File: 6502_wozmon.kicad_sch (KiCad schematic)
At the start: 37 parts, among them J1 Barrel_Jack_Switch_Pin3Ring, J2 DB9_Female, J3 "Switch", J4 Conn_01x08_Male, U1 7400, U2 W65C02, U3 28C256, U4 W65C51N, U5 62256, U6 MAX232, U7 65C22, U8 WC1602A, X1 GTXO-S14V, Y1 1.8432MHZ

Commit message: schematic updated to include debounced reset section; added barrel connector.
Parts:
- removed C1: 0.1u, Capacitor_THT:C_Disc_D5.0mm_W2.5mm_P5.00mm, symbol Device:C
- removed J3: "Switch", Connector_PinHeader_2.54mm:PinHeader_1x03_P2.54mm_Vertical, symbol Connector:Conn_01x03_Male
- removed R1: 1K, Resistor_THT:R_Axial_DIN0207_L6.3mm_D2.5mm_P10.16mm_Horizontal, symbol Device:R
- added C? (x2): C, symbol Device:C
- added C?: 10u, symbol Device:C
- added D?: LED, symbol Device:LED
- added J? (x2): Conn_01x03_Male, symbol Connector:Conn_01x03_Male
- added R?: 10K, symbol Device:R
- added R?: 330, symbol Device:R
- added R?: 1K, symbol Device:R
- added U? (x7): 74HC14, symbol 74xx:74HC14
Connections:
- net +5V: now also C?.1, C?.1, R?.2, U?.14 (VCC)
- net CLK: now also J4.1 (Pin_1); no longer J4.5 (Pin_5)
- net GND: now also J4.5 (Pin_5), J4.6 (Pin_6), J4.7 (Pin_7), J4.8 (Pin_8), C?.2, C?.2, C?.2, D?.1 (K), J?.3 (Pin_3), U?.11, U?.13, U?.5, U?.7 (GND), U?.9; no longer J4.1 (Pin_1), J4.2 (Pin_2), J4.3 (Pin_3), J4.4 (Pin_4)
- net RESET*: now also J4.2 (Pin_2), U?.4
- net TXD: now also J4.4 (Pin_4)
- net XTAL: no longer J4.6 (Pin_6)
- net MAX232_12: now reaches R7.1, U4.12 (RxD), U6.12 (R1OUT)
- net MAX232_12: now also J4.3 (Pin_3)
- new net: J?.1 (Pin_1), R?.1 (x2)
- new net: D?.2 (A), R?.2
- new net: R?.1, U?.2, U?.3
- new net: C?.1, R?.2, U?.1
- no-connect marks 48 -> 50
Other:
- note added: "DEBOUNCED RESET SECTION"
- note added: "Jx and Jy REPRESENT A FOUR-PIN BUTTON."
- moved on the sheet: J2, J4, U1D, U1E

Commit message: increment
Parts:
- removed LED_3, LED_4: LED, LED_THT:LED_D5.0mm, symbol Device:LED
- removed R7, R8: 220, Resistor_THT:R_Axial_DIN0207_L6.3mm_D2.5mm_P10.16mm_Horizontal, symbol Device:R
- C1, C10, C11: renamed from C?; footprint (none) -> Capacitor_THT:C_Disc_D5.0mm_W2.5mm_P5.00mm
- D3: renamed from D?; footprint (none) -> LED_THT:LED_D5.0mm
- J3, J5: renamed from J?; footprint (none) -> Connector_PinHeader_2.54mm:PinHeader_1x03_P2.54mm_Vertical
- R1, R6, R7: renamed from R?; footprint (none) -> Resistor_THT:R_Axial_DIN0207_L6.3mm_D2.5mm_P10.16mm_Horizontal
- U3: footprint Package_DIP:DIP-28_W15.24mm_Socket -> Socket:DIP_Socket-28_W11.9_W12.7_W15.24_W17.78_W18.5_3M_228-1277-00-0602J
- U5: footprint Socket:DIP_Socket-28_W11.9_W12.7_W15.24_W17.78_W18.5_3M_228-1277-00-0602J -> Package_DIP:DIP-28_W15.24mm_Socket
- U9: renamed from U?; footprint (none) -> Package_DIP:DIP-14_W7.62mm_Socket

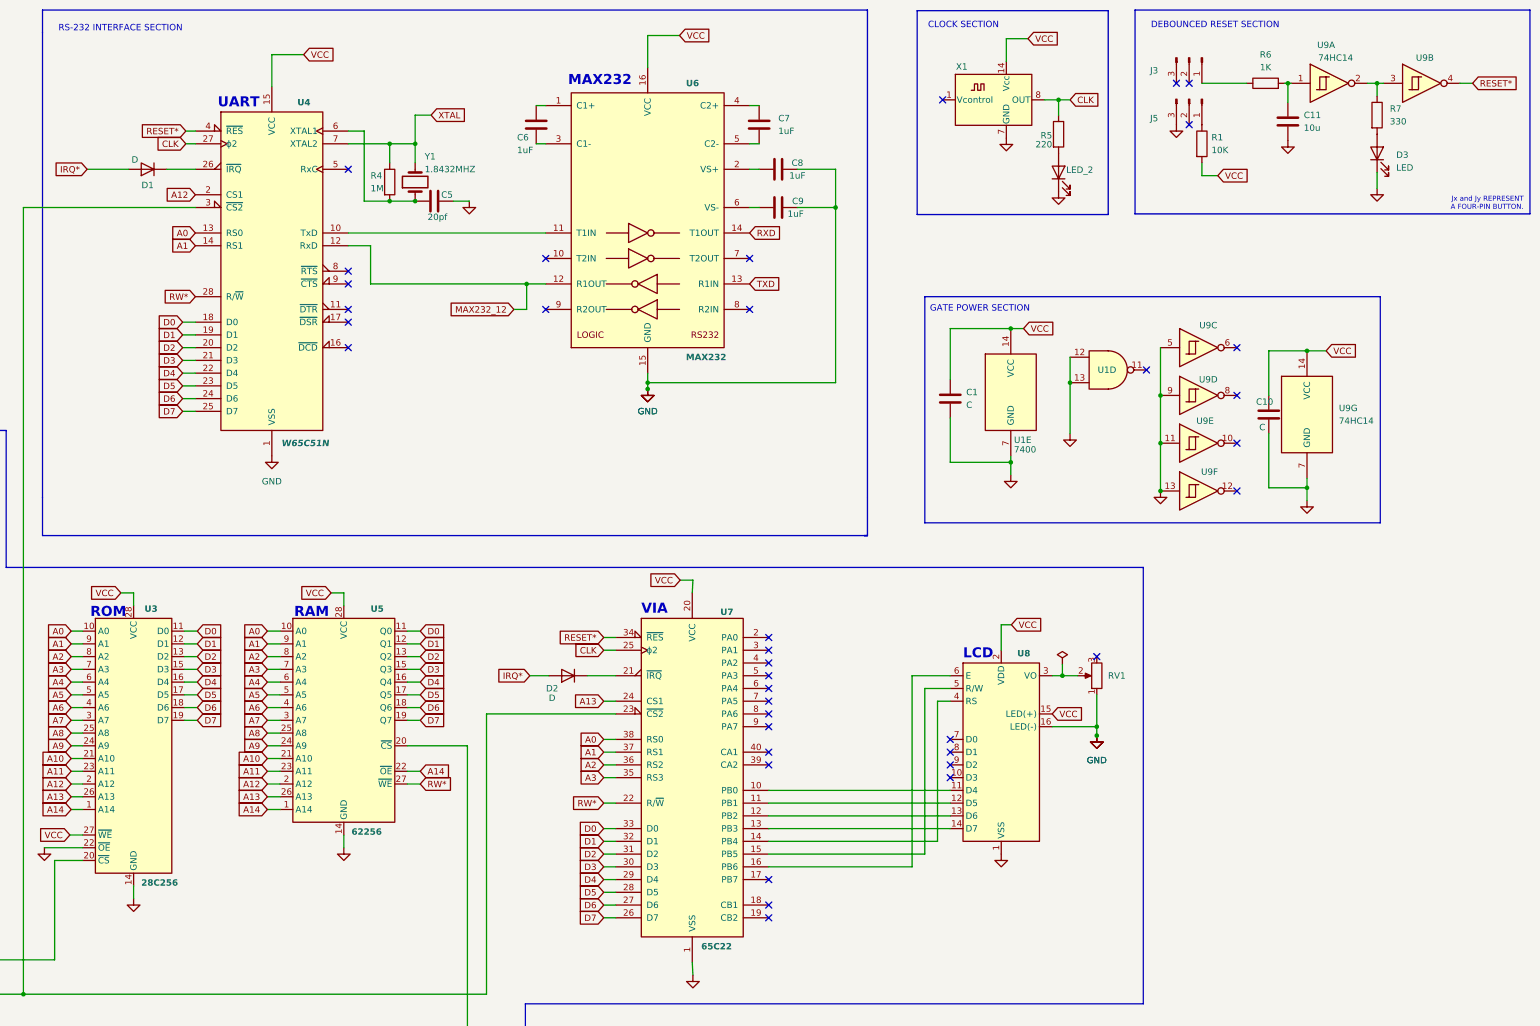
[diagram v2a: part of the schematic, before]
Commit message: 1.  Updated Files     A.  The pin headers being used as a switch were replaced with a proper button switch and footprint.         a.  The following were updated:             1.  6502_wozmon.kicad_pcb 	        2.  6502_wozmon.kicad_prl 2.  Notes     A.  The silkscreen for the RAM and ROM chips is reversed.         a.  This is becuase the footprints are reversed in the schematic editor.             1.  I switched the footprints, but this caused *37& clearance violations in the PCB editor.             2.  Fixing this would have required *substantial* re-routing.             3.  I decided for forego fixing this; I will accept this minor issue on the silkscreen.
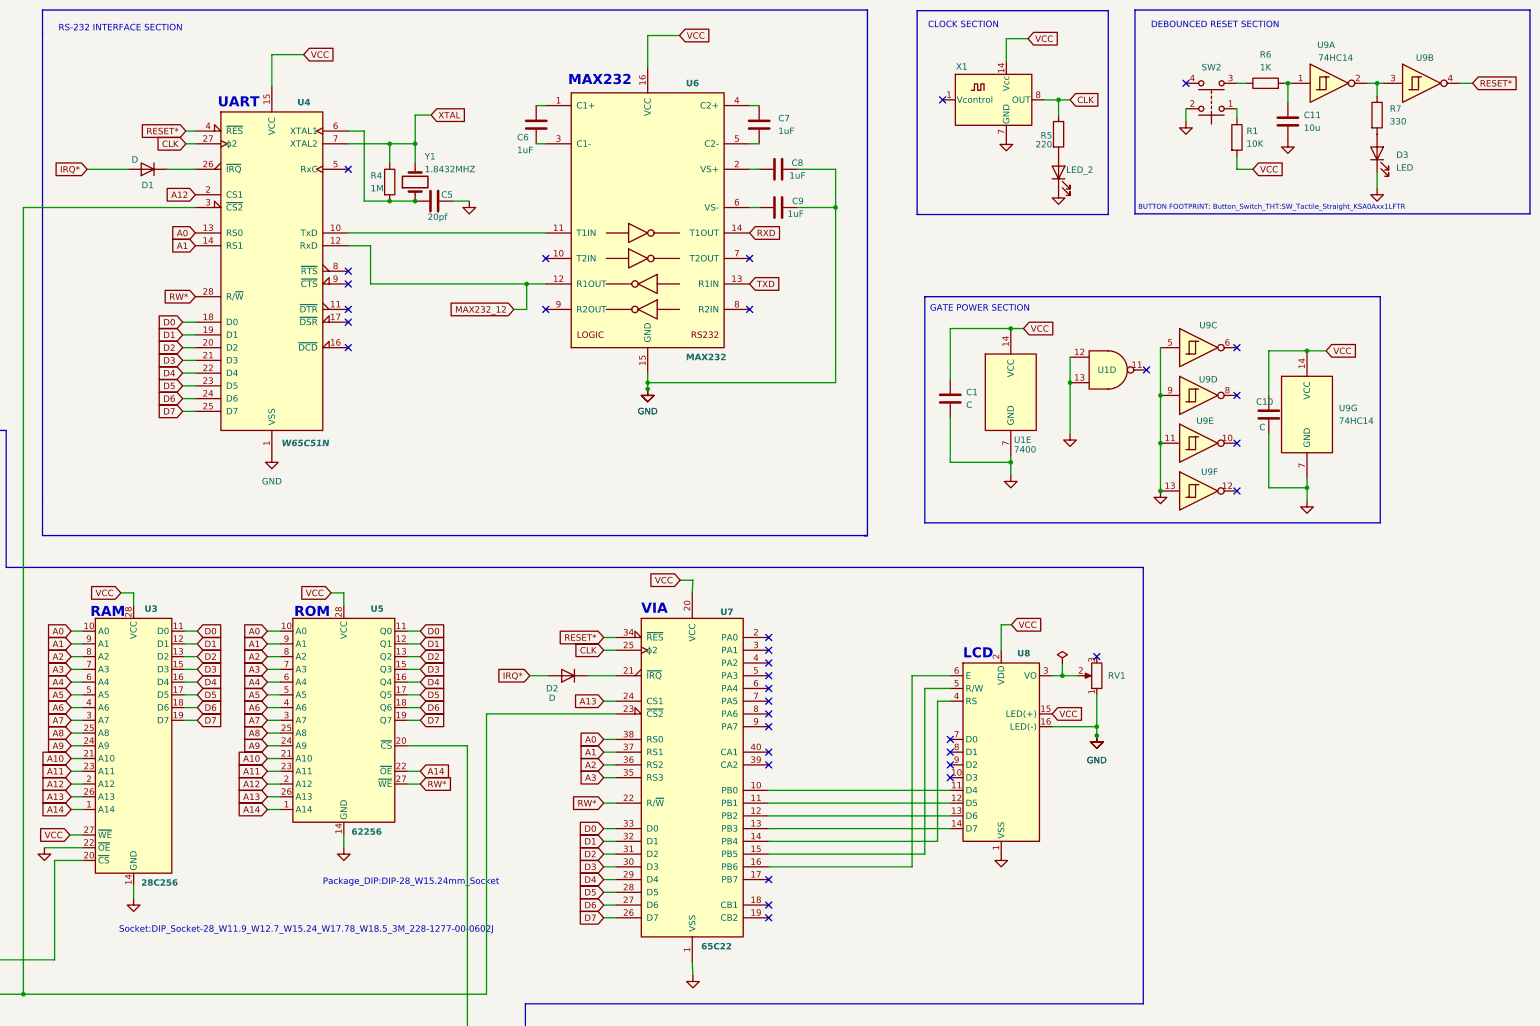
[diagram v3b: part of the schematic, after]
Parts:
- removed J3, J5: Conn_01x03_Male, Connector_PinHeader_2.54mm:PinHeader_1x03_P2.54mm_Vertical, symbol Connector:Conn_01x03_Male
- added SW2: SW_Push_Dual, Button_Switch_THT:SW_Tactile_Straight_KSA0Axx1LFTR, symbol Switch:SW_Push_Dual
- U3: footprint Socket:DIP_Socket-28_W11.9_W12.7_W15.24_W17.78_W18.5_3M_228-1277-00-0602J -> Package_DIP:DIP-28_W15.24mm_Socket
- U5: footprint Package_DIP:DIP-28_W15.24mm_Socket -> Socket:DIP_Socket-28_W11.9_W12.7_W15.24_W17.78_W18.5_3M_228-1277-00-0602J
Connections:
- net GND: now also SW2.2
- net at R1.1: now also SW2.1
- net at R6.1: now also SW2.3
- no-connect marks 50 -> 48
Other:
- note added: "BUTTON FOOTPRINT: Button_Switch_THT:SW_Tactile_Straight_KSA0Axx1LFTR"
- note added: "Package_DIP:DIP-28_W15.24mm_Socket"
- note added: "Socket:DIP_Socket-28_W11.9_W12.7_W15.24_W17.78_W18.5_3M_228-1277-00-0602J"
- note removed: "Jx and Jy REPRESENT A FOUR-PIN BUTTON."
- moved on the sheet: R1

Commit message: Added gerber files.
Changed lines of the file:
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@@
     (stroke (width 0) (type default) (color 0 0 0 0))
   )
-  (text "Package_DIP:DIP-28_W15.24mm_Socket" (at 177.8 192.405 0)
+  (text "Package_DIP:DIP-28_W15.24mm_Socket" (at 183.515 185.42 0)
     (effects (font (size 1.27 1.27)) (justify left bottom))
   )
@@
   )
   (text "Socket:DIP_Socket-28_W11.9_W12.7_W15.24_W17.78_W18.5_3M_228-1277-00-0602J"
-    (at 137.16 201.93 0)
+    (at 141.605 195.58 0)
     (effects (font (size 1.27 1.27)) (justify left bottom))
   )

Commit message: Added README.md, photos, and sotware files.
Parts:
- C1, C10: value C -> 0.1u
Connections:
- net GND: now also J1.2, SW2.3; no longer SW2.2
- net at R6.1: now also SW2.2; no longer SW2.3
- no-connect marks 48 -> 47
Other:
- note added: "BRANCH : 20240818"
- note added: "FOOTPRINT: Package_DIP:DIP-28_W15.24mm_Socket"
- note added: "RS-232 BAUD RATE: 19200 8N1"
- note removed: "Package_DIP:DIP-28_W15.24mm_Socket"
- note removed: "Socket:DIP_Socket-28_W11.9_W12.7_W15.24_W17.78_W18.5_3M_228-1277-00-0602J"
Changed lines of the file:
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@@
   (junction (at 191.135 55.88) (diameter 0) (color 0 0 0 0)
   )
+  (junction (at 30.48 34.29) (diameter 0) (color 0 0 0 0)
+  )
   (junction (at 64.135 31.75) (diameter 0) (color 0 0 0 0)
   )
@@
   (no_connect (at 342.011 89.535))
   (no_connect (at 266.7 142.875))
-  (no_connect (at 28.575 34.29))
   (no_connect (at 70.485 132.715))
   (no_connect (at 302.895 165.735))
@@
     (stroke (width 0) (type default) (color 0 0 0 0))
   )
-  (wire (pts (xy 360.045 32.385) (xy 361.95 32.385))
-    (stroke (width 0) (type default) (color 0 0 0 0))
-  )
   (wire (pts (xy 100.965 170.815) (xy 103.759 170.815))
     (stroke (width 0) (type default) (color 0 0 0 0))
@@
     (stroke (width 0) (type default) (color 0 0 0 0))
   )
+  (wire (pts (xy 349.885 37.465) (xy 347.98 37.465))
+    (stroke (width 0) (type default) (color 0 0 0 0))
+  )
   (wire (pts (xy 58.039 160.655) (xy 60.579 160.655))
     (stroke (width 0) (type default) (color 0 0 0 0))
@@
     (stroke (width 0) (type default) (color 0 0 0 0))
   )
+  (wire (pts (xy 28.575 34.29) (xy 30.48 34.29))
+    (stroke (width 0) (type default) (color 0 0 0 0))
+  )
   (polyline (pts (xy 285.75 122.555) (xy 286.385 122.555))
     (stroke (width 0) (type default) (color 0 0 0 0))
@@
     (stroke (width 0) (type default) (color 0 0 0 0))
   )
+  (wire (pts (xy 347.98 27.305) (xy 361.95 27.305))
+    (stroke (width 0) (type default) (color 0 0 0 0))
+  )
   (wire (pts (xy 218.44 72.39) (xy 222.25 72.39))
     (stroke (width 0) (type default) (color 0 0 0 0))
@@
     (stroke (width 0) (type default) (color 0 0 0 0))
   )
-  (wire (pts (xy 349.885 37.465) (xy 349.885 40.005))
-    (stroke (width 0) (type default) (color 0 0 0 0))
-  )
   (wire (pts (xy 360.045 46.99) (xy 360.045 49.53))
     (stroke (width 0) (type default) (color 0 0 0 0))
@@
     (stroke (width 0) (type default) (color 0 0 0 0))
   )
+  (wire (pts (xy 347.98 37.465) (xy 347.98 27.305))
+    (stroke (width 0) (type default) (color 0 0 0 0))
+  )
   (wire (pts (xy 332.105 160.655) (xy 323.215 160.655))
     (stroke (width 0) (type default) (color 0 0 0 0))
@@
     (stroke (width 0) (type default) (color 0 0 0 0))
   )
+  (wire (pts (xy 361.95 27.305) (xy 361.95 32.385))
+    (stroke (width 0) (type default) (color 0 0 0 0))
+  )
   (wire (pts (xy 280.035 49.53) (xy 280.035 57.15))
     (stroke (width 0) (type default) (color 0 0 0 0))
@@
     (stroke (width 0) (type default) (color 0 0 0 0))
   )
+  (wire (pts (xy 360.045 32.385) (xy 360.045 33.655))
+    (stroke (width 0) (type default) (color 0 0 0 0))
+  )
   (wire (pts (xy 129.921 151.765) (xy 127.635 151.765))
     (stroke (width 0) (type default) (color 0 0 0 0))
@@
     (stroke (width 0) (type default) (color 0 0 0 0))
   )
-  (text "Package_DIP:DIP-28_W15.24mm_Socket" (at 183.515 185.42 0)
+  (text "FOOTPRINT: \nPackage_DIP:DIP-28_W15.24mm_Socket" (at 183.515 187.325 0)
     (effects (font (size 1.27 1.27)) (justify left bottom))
   )
@@
     (effects (font (size 1.27 1.27)) (justify left bottom))
   )
-  (text "Socket:DIP_Socket-28_W11.9_W12.7_W15.24_W17.78_W18.5_3M_228-1277-00-0602J"
-    (at 141.605 195.58 0)
+  (text "FOOTPRINT: \nPackage_DIP:DIP-28_W15.24mm_Socket" (at 141.605 197.485 0)
     (effects (font (size 1.27 1.27)) (justify left bottom))
   )
@@
     (effects (font (size 2 2) bold) (justify left bottom))
   )
+  (text "BRANCH : 20240818" (at 51.435 66.675 0)
+    (effects (font (size 1.27 1.27)) (justify left bottom))
+  )
   (text "GATE POWER SECTION" (at 298.831 78.105 0)
     (effects (font (size 1.27 1.27)) (justify left bottom))
   )
-  (text "RAM" (at 131.445 139.065 0)
+  (text "ROM" (at 131.445 139.065 0)
     (effects (font (size 2 2) bold) (justify left bottom))
   )
@@
     (effects (font (size 1 1)) (justify left bottom))
   )
-  (text "ROM" (at 172.085 139.065 0)
+  (text "RAM" (at 172.085 139.065 0)
     (effects (font (size 2 2) bold) (justify left bottom))
   )
@@
     (effects (font (size 2 2) bold) (justify left bottom))
   )
+  (text "RS-232 BAUD RATE:  19200 8N1" (at 106.68 66.675 180)
+    (effects (font (size 1.27 1.27)) (justify right bottom))
+  )
   (global_label "A15" (shape input) (at 71.247 221.615 180) (fields_autoplaced)
     (effects (font (size 1.27 1.27)) (justify right))
@@
       (effects (font (size 1.27 1.27)) (justify left))
     )
-    (property "Value" "C" (id 1) (at 364.49 100.965 0)
+    (property "Value" "0.1u" (id 1) (at 364.49 100.965 0)
       (effects (font (size 1.27 1.27)) (justify left))
     )
@@
   (symbol (lib_id "Connector:DB9_Female") (at 98.425 34.29 0) (unit 1)
     (in_bom yes) (on_board yes)
-    (property "Reference" "J2" (id 0) (at 94.615 50.8 0)
+    (property "Reference" "J2" (id 0) (at 93.98 49.53 0)
       (effects (font (size 1.27 1.27)) (justify left))
     )
-    (property "Value" "DB9_Female" (id 1) (at 92.71 53.975 0)
+    (property "Value" "DB9_Female" (id 1) (at 93.98 52.07 0)
       (effects (font (size 1.27 1.27)) (justify left))
     )
@@
       (effects (font (size 1.27 1.27)) (justify left))
     )
-    (property "Value" "C" (id 1) (at 306.07 96.5199 0)
+    (property "Value" "0.1u" (id 1) (at 306.07 96.5199 0)
       (effects (font (size 1.27 1.27)) (justify left))
     )
@@
     (pin "2")
   )
-  (symbol (lib_id "power:GND") (at 349.885 40.005 0) (unit 1)
+  (symbol (lib_id "power:GND") (at 360.045 33.655 0) (unit 1)
     (in_bom yes) (on_board yes) (fields_autoplaced)
-    (property "Reference" "#PWR0105" (id 0) (at 349.885 46.355 0)
+    (property "Reference" "#PWR0105" (id 0) (at 360.045 40.005 0)
       (effects (font (size 1.27 1.27)) hide)
     )
-    (property "Value" "GND" (id 1) (at 349.885 45.085 0)
+    (property "Value" "GND" (id 1) (at 360.045 38.735 0)
       (effects (font (size 1.27 1.27)) hide)
     )
-    (property "Footprint" "" (id 2) (at 349.885 40.005 0)
+    (property "Footprint" "" (id 2) (at 360.045 33.655 0)
       (effects (font (size 1.27 1.27)) hide)
     )
-    (property "Datasheet" "" (id 3) (at 349.885 40.005 0)
+    (property "Datasheet" "" (id 3) (at 360.045 33.655 0)
       (effects (font (size 1.27 1.27)) hide)
     )
@@
     )
     (path "/84547bf0-2070-4091-8aa1-b1fca7d4f424"
-      (reference "C1") (unit 1) (value "C") (footprint "Capacitor_THT:C_Disc_D5.0mm_W2.5mm_P5.00mm")
+      (reference "C1") (unit 1) (value "0.1u") (footprint "Capacitor_THT:C_Disc_D5.0mm_W2.5mm_P5.00mm")
     )
     (path "/dec760bc-2d91-4812-af91-a8a352a1e17d"
@@
     )
     (path "/10db89f4-e945-464e-9220-3f1319291140"
-      (reference "C10") (unit 1) (value "C") (footprint "Capacitor_THT:C_Disc_D5.0mm_W2.5mm_P5.00mm")
+      (reference "C10") (unit 1) (value "0.1u") (footprint "Capacitor_THT:C_Disc_D5.0mm_W2.5mm_P5.00mm")
     )
     (path "/f7ed009b-059d-4e27-985b-41ee3239f67f"
